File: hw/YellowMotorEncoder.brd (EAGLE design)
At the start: 35 x 22.4 mm, 20 parts, among them P1 M1

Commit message: Finish routing of the board
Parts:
- moved R3 18.6 mm to (10.0, 2.50)
- moved R1 18.6 mm to (23.0, 20.0)
- moved LED_POWER 18.5 mm to (19.0, 20.0)
- moved R2 18.1 mm to (10.0, 20.0)
- moved LED_B 16.0 mm to (14.0, 2.50), turned to 90 degrees
- moved LED_A 15.5 mm to (14.0, 20.0), turned to 90 degrees
- moved C2 6.74 mm to (7.50, 12.8), turned to 0 degrees
- moved R4 6.71 mm to (14.0, 18.0)
- moved R5 6.41 mm to (14.0, 4.25)
- moved C7 6.02 mm to (4.50, 11.0), turned to 180 degrees
- moved C1 5.77 mm to (7.50, 7.75), turned to 0 degrees
- moved U$2 5.50 mm to (4.60, 8.70)
- moved U$1 4.40 mm to (4.60, 13.8)
- moved C6 3.72 mm to (4.50, 16.2), turned to 180 degrees
- moved C4 0.40 mm to (27.9, 3.20)
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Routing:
- net VCC: track 0.00 -> 67.8 mm, vias 0 -> 6
- net B: track 0.00 -> 34.4 mm
- net A: track 0.00 -> 30.8 mm
- net LED_POWER: track 0.00 -> 2.53 mm
- net LED_TOP1: track 0.00 -> 2.53 mm
- net LED_SIDE1: track 0.00 -> 2.53 mm
- added copper zone on layer 16, net GND
- added copper zone on layer 1, net M-
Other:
- board text added: "M+ E+ A B E- M-"
- board text added: "MotorEncoder"
- board text added: "YellowMotorEncoder"
- board text added: "github::roboticsbrno/RB0003-YellowMotorEncoder"
- board text added: "v1.0"
- board text added: "v1.1"

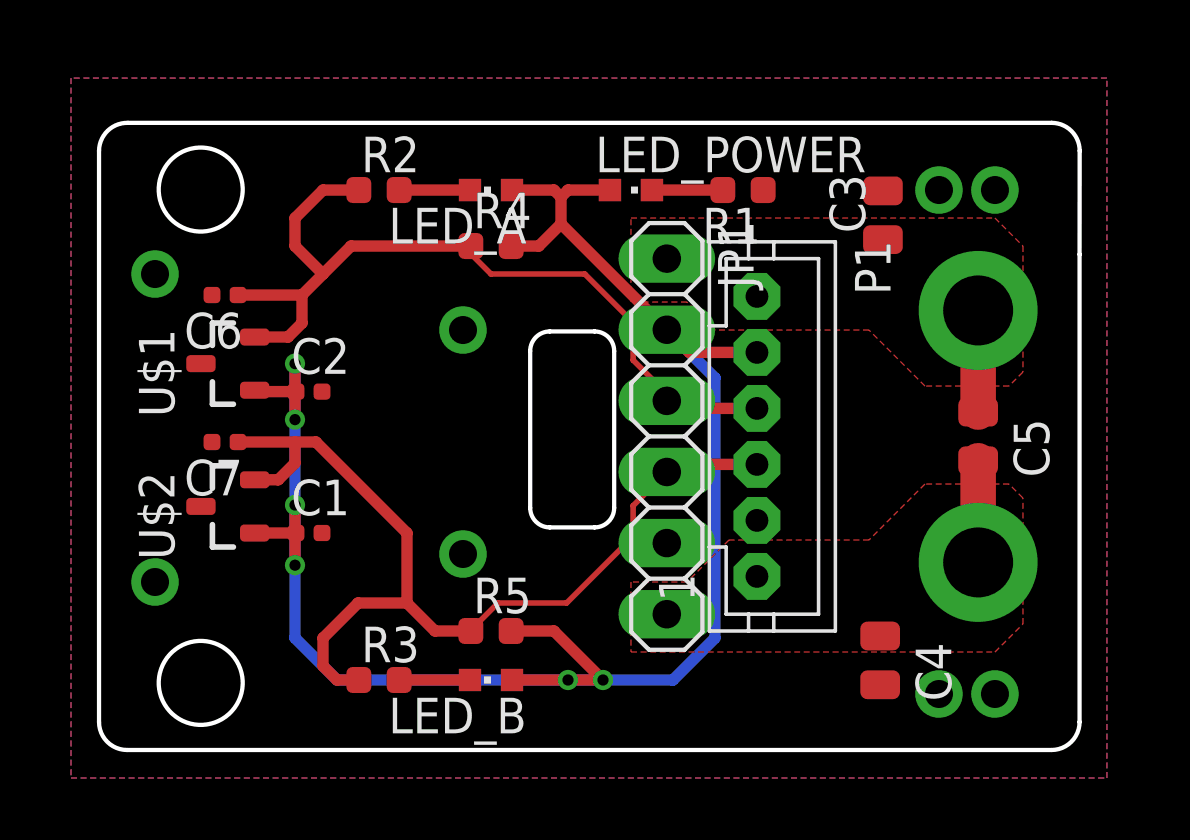
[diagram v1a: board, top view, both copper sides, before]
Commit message: Finish routing YellowMotorEncoder v1.0
- route PCB
- correct position of mounting holes
- fix connectors signal
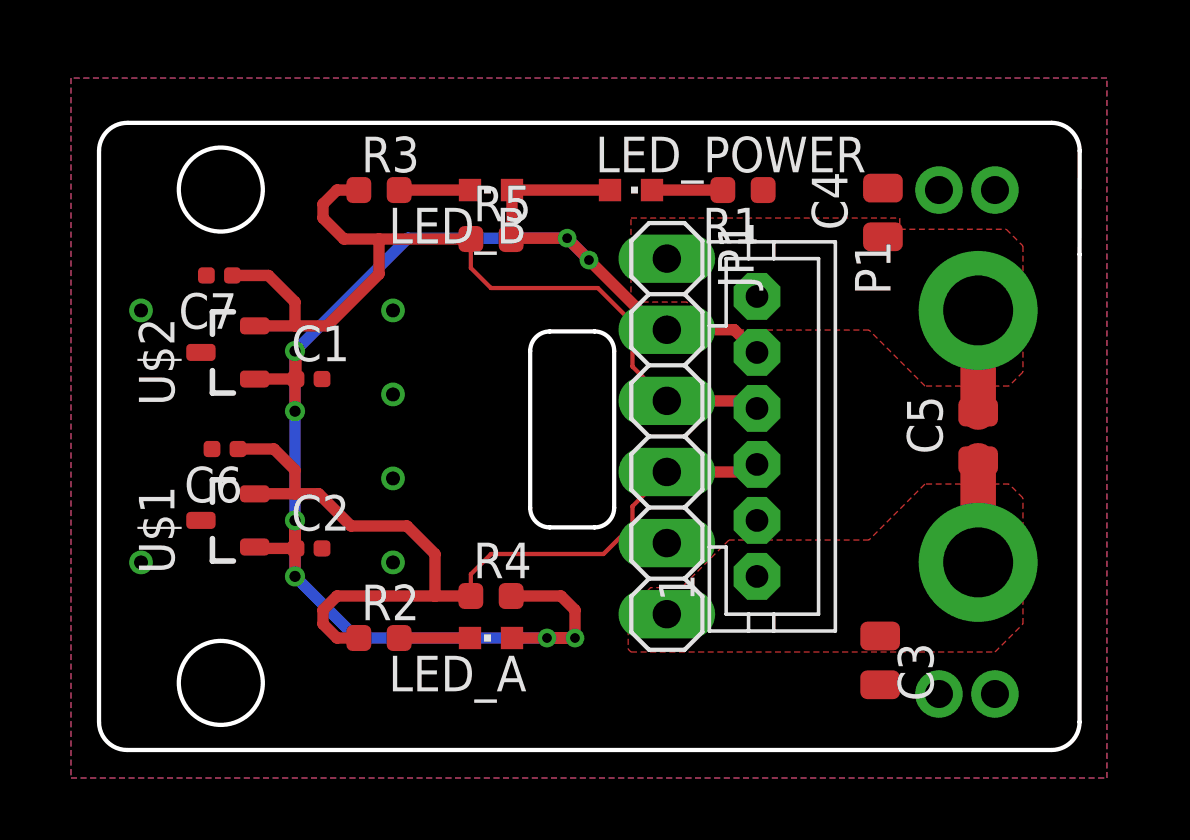
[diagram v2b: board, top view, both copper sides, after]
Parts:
- C3, C4, C5: value 330p/50V -> 330n/50V
- moved LED_B 17.5 mm to (14.0, 20.0)
- moved R3 17.5 mm to (10.0, 20.0)
- moved C4 16.0 mm to (28.0, 19.2), turned to 90 degrees
- moved LED_A 16.0 mm to (14.0, 4.00)
- moved R2 16.0 mm to (10.0, 4.00)
- moved C3 15.9 mm to (27.9, 3.20), turned to 270 degrees
- moved R5 14.0 mm to (14.0, 18.2)
- moved R4 12.5 mm to (14.0, 5.50)
- moved C7 5.95 mm to (4.30, 16.9)
- moved U$1 5.60 mm to (4.60, 8.20)
- moved C2 5.60 mm to (7.50, 7.20)
- moved C1 5.50 mm to (7.50, 13.2)
- moved C6 5.50 mm to (4.50, 10.8)
- moved U$2 5.50 mm to (4.60, 14.2)
- turned C5 to 90 degrees
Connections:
- net A: now also JP1.4, P1.3; no longer JP1.3, P1.4
- net B: now also JP1.3, P1.4; no longer JP1.4, P1.3
- net M+: now also JP1.6, P1.1, U$3.P$2; no longer JP1.1, P1.6, U$3.P$1
- net M-: now also JP1.1, P1.6, U$3.P$1; no longer JP1.6, P1.1, U$3.P$2
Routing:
- net B: track 34.4 -> 31.8 mm
- net VCC: track 67.8 -> 66.0 mm, vias 6 -> 8
- net A: track 30.8 -> 32.5 mm
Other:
- outline, holes or cut-outs redrawn
- board text added: "M- VCC B A GND M+"
- board text added: "github::roboticsbrno/ RB0003-YellowMotorEncoder"
- board text added: "v1.0 CC BY-SA 4.0"
- board text removed: "+"
- board text removed: "-"
- board text removed: "M+"
- board text removed: "M+ E+ A B E- M-"
- board text removed: "M-"
- board text removed: "MotorEncoder"
- board text removed: "github::roboticsbrno/RB0003-YellowMotorEncoder"
- board text removed: "v1.0"
- board text removed: "v1.1"

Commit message: Swap encoder power polarity
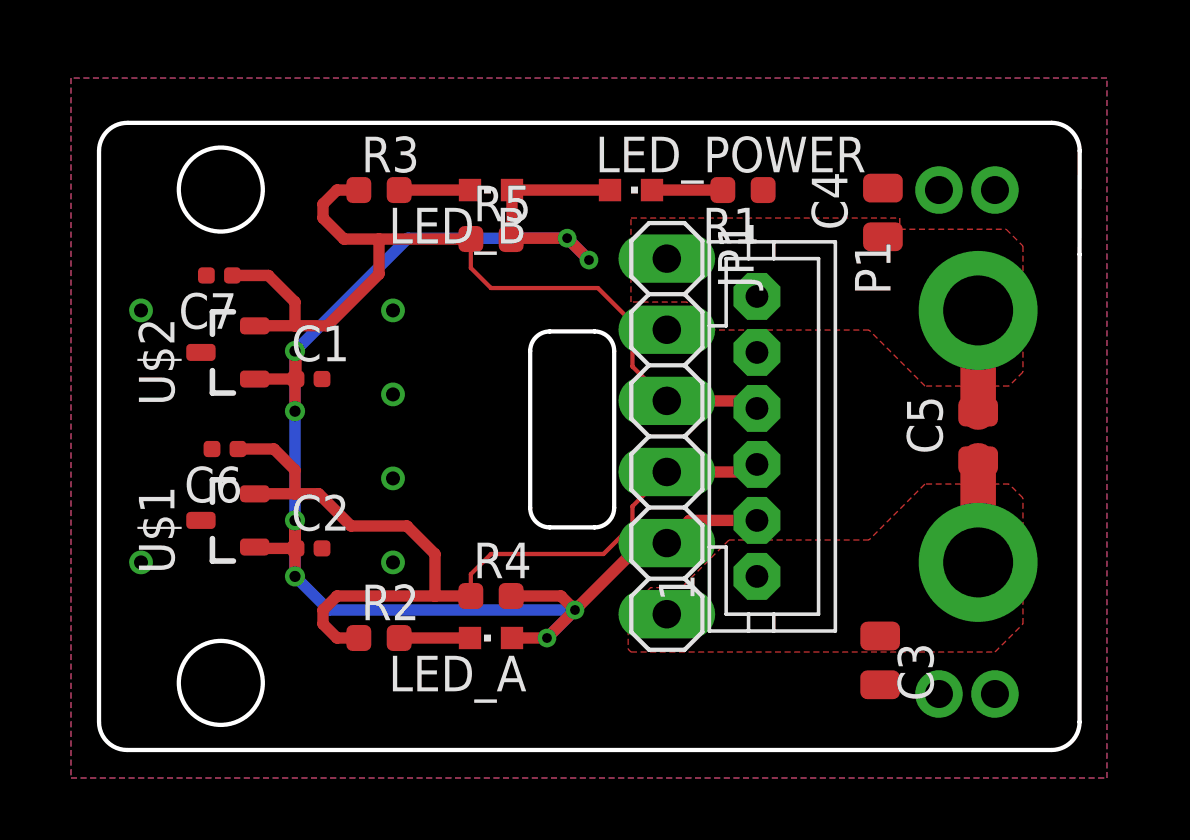
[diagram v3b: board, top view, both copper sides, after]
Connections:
- net GND: now also JP1.2, P1.5; no longer JP1.5, P1.2
- net VCC: now also JP1.5, P1.2; no longer JP1.2, P1.5
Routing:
- net VCC: track 66.0 -> 64.9 mm

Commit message: Fixed LEDs orientation
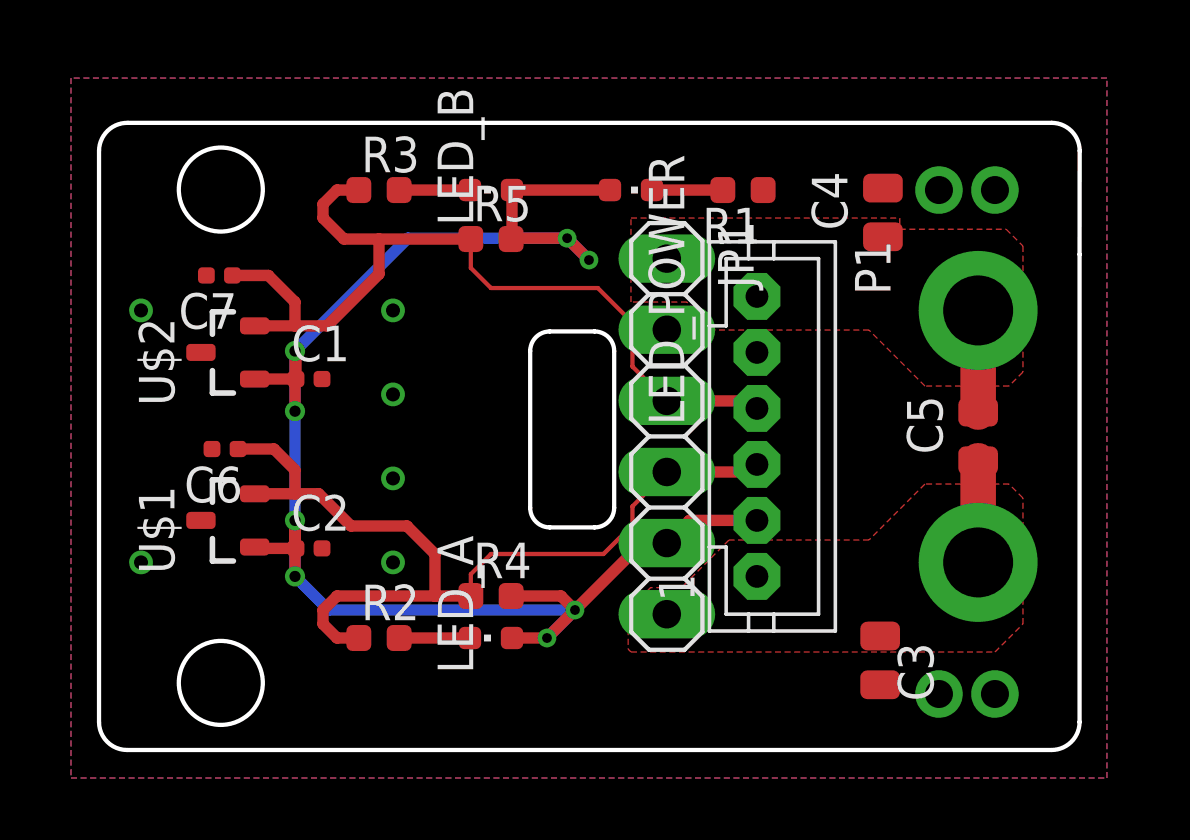
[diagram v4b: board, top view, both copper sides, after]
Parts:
- turned LED_A to 0 degrees
- turned LED_B to 0 degrees
- turned LED_POWER to 180 degrees

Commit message: Rerouted board
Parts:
- moved R1 21.2 mm to (3.70, 11.2), turned to 0 degrees
- moved LED_POWER 14.8 mm to (7.10, 11.2), turned to 0 degrees
- moved R3 6.71 mm to (16.0, 17.0)
- moved R2 6.32 mm to (16.0, 6.00)
- moved C7 5.03 mm to (8.80, 14.7), turned to 270 degrees
- moved C6 4.76 mm to (8.80, 8.70), turned to 270 degrees
- moved C3 3.64 mm to (31.4, 2.20)
- moved C4 3.64 mm to (31.5, 20.2)
- moved LED_B 2.24 mm to (16.0, 19.0), turned to 180 degrees
- moved LED_A 2.00 mm to (16.0, 4.00), turned to 180 degrees
- moved R4 1.12 mm to (13.0, 5.00), turned to 270 degrees
- moved R5 1.03 mm to (13.0, 18.0), turned to 90 degrees
- moved C2 0.54 mm to (7.30, 7.70), turned to 90 degrees
- moved C1 0.49 mm to (7.30, 13.7), turned to 90 degrees
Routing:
- net VCC: track 64.9 -> 51.7 mm, vias 8 -> 3
- net B: track 31.8 -> 26.1 mm
- net A: track 32.5 -> 27.5 mm
- net LED_TOP1: track 2.53 -> 3.94 mm
- net LED_SIDE1: track 2.53 -> 3.94 mm
- net LED_POWER: track 2.53 -> 1.93 mm
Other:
- board text added: "M- GND B A VCC M+"
- board text removed: "M- VCC B A GND M+"
